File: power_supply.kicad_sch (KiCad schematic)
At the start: 24 parts, among them U3 ST1S10PHR, U4 ST1S09IPUR

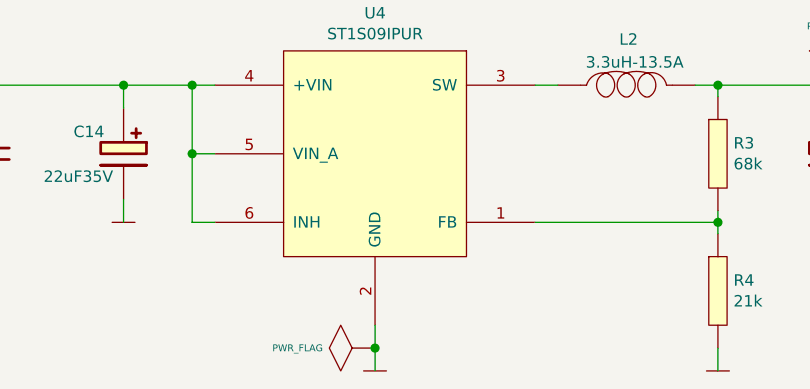
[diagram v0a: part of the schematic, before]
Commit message: Cleared all errors DRC
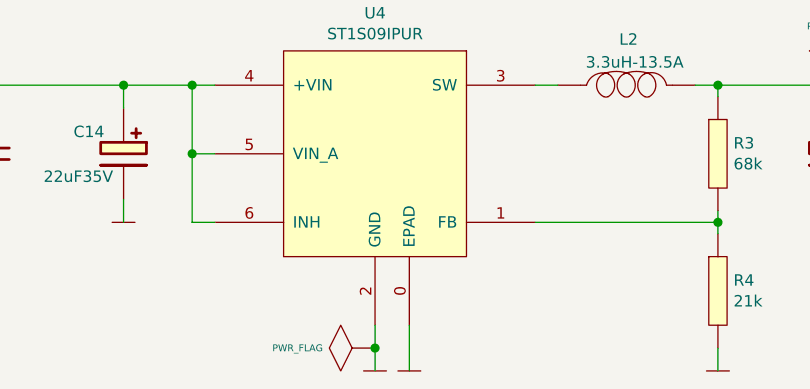
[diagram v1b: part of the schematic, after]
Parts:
- C15: symbol Capacitors_Smd0603:10nF_0603 -> Capacitors_Smd0603:10nF; Supplier TME -> Tme
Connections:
- net GND: now also U4.0 (EPAD)
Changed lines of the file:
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@@
     (stroke (width 0) (type solid) (color 0 0 0 0))
+  )
+  (wire (pts (xy 217.17 186.69) (xy 217.17 191.77))
+    (stroke (width 0) (type default) (color 0 0 0 0))
   )
   (wire (pts (xy 266.7 118.11) (xy 266.7 119.38))
@@
       (effects (font (size 1.27 1.27)) hide)
     )
+    (pin "0")
     (pin "1")
     (pin "2")
@@
     (pin "8")
   )
-  (symbol (lib_id "Capacitors_Smd0603:10nF_0603") (at 251.46 110.49 0) (unit 1)
+  (symbol (lib_id "Capacitors_Smd0603:10nF") (at 251.46 110.49 0) (unit 1)
     (in_bom yes) (on_board yes)
     (property "Reference" "C15" (id 0) (at 254.7874 109.3216 0)
@@
       (effects (font (size 1.27 1.27)) hide)
     )
-    (property "Supplier" "TME" (id 6) (at 251.46 110.49 0)
+    (property "Supplier" "Tme" (id 6) (at 251.46 110.49 0)
       (effects (font (size 1.27 1.27)) hide)
     )
@@
       (effects (font (size 1.524 1.524)))
     )
+    (pin "1")
+  )
+  (symbol (lib_id "power:GND_NO_GLOBAL") (at 217.17 191.77 0) (unit 1)
+    (in_bom yes) (on_board yes)
+    (property "Reference" "#PWR233" (id 0) (at 217.17 189.23 0)
+      (effects (font (size 0.762 0.762)) hide)
+    )
+    (property "Value" "GND_NO_GLOBAL" (id 1) (at 217.17 194.31 0)
+      (effects (font (size 0.762 0.762)) hide)
+    )
+    (property "Footprint" "" (id 2) (at 217.17 191.77 0)
+      (effects (font (size 1.524 1.524)))
+    )
+    (property "Datasheet" "" (id 3) (at 217.17 191.77 0)
+      (effects (font (size 1.524 1.524)))
+    )

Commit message: Eliminated all warnings realted with footprints
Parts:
- C10, C13, C19, C20, C7, C9: footprint Capacitors_Smd_0603:100nF_0603 -> Capacitors_Smd_0402:100nF_0402; symbol Capacitors_Smd0603:100n -> Capacitors_Smd0402:100nF; Developer (none) -> MW; LCSC Part # (optional) (none) -> C131394; Manufacturer SAMSUNG -> Murata; Manufacturer Part Number CL10B104JB8NNNC -> GRM155R71H104KE14D; Package 0603 -> 0402; Package_1 (none) -> 0402; Price@1000pcs 0,02231 -> 0,03299; Price@1pc 0,04540 -> 0,07091; Supplier TME -> Tme; Supplier Part Number CL10B104JB8NNNC -> GRM155R71H104KE14D; URL https://www.tme.eu/pl/details/cl10b104jb8nnnc/kondensatory-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 -> https://www.tme.eu/pl/details/grm155r71h104ke14d/kondensato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

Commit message: Gerbers created, BOM, CPL
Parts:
- R2, R6: Price@1pc (none) -> 0,07119
- R3: Developer (none) -> MW; Field11 MW -> (none)
- R4: Price@1pc (none) -> 0,05002
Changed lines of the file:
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@@
+      (effects (font (size 1.27 1.27)) hide)
+    )
+    (property "Price@1pc" "0,07119" (id 14) (at 266.7 125.73 0)
       (effects (font (size 1.27 1.27)) hide)
     )
@@
       (effects (font (size 1.27 1.27)) hide)
     )
-    (property "Datasheet" "Resistors/Smd_0603/Components_Documentation/Vishay_Resistors_SM0603.pdf" (id 3) (at 262.89 121.92 0)
+    (property "Datasheet" "https://www.tme.eu/Document/b315665a56acbc42df513c99b390ad98/ROYALOHM-THICKFILM.pdf" (id 3) (at 262.89 121.92 0)
       (effects (font (size 1.27 1.27)) hide)
     )
@@
     )
     (property "LCSC Part #(optional)" "C234435" (id 13) (at 186.69 114.3 0)
+      (effects (font (size 1.27 1.27)) hide)
+    )
+    (property "Price@1pc" "0,07119" (id 14) (at 186.69 114.3 0)
       (effects (font (size 1.27 1.27)) hide)
     )
@@
       (effects (font (size 1.27 1.27)) hide)
     )
+    (property "Price@1pc" "0,05002" (id 14) (at 251.46 182.88 0)
+      (effects (font (size 1.27 1.27)) hide)
+    )
     (pin "1")
     (pin "2")
@@
     )
     (property "Package" "7.2 mm x 6.65 mm x 3 mm" (id 12) (at 241.3 160.02 0)
-      (effects (font (size 1.27 1.27)) hide)
-    )
-    (pin "1")
-    (pin "2")
-  )
-  (symbol (lib_id "Resistors_Smd0603:68k") (at 251.46 167.64 0) (unit 1)
-    (in_bom yes) (on_board yes)
-    (property "Reference" "R3" (id 0) (at 253.1872 166.4716 0)
-      (effects (font (size 1.27 1.27)) (justify left))
-    )
-    (property "Value" "68k" (id 1) (at 253.1872 168.783 0)
-      (effects (font (size 1.27 1.27)) (justify left))
-    )
-    (property "Footprint" "Resistor_Smd_0603:68k_0603" (id 2) (at 251.46 179.07 0)
-      (effects (font (size 1.27 1.27)) hide)
-    )
-    (property "Datasheet" "Resistors/Smd_0603/Components_Documentation/Vishay_Resistors_SM0603.pdf" (id 3) (at 251.46 179.07 0)
-      (effects (font (size 1.27 1.27)) hide)
-    )
-    (property "Manufacturer" "ROYAL OHM" (id 4) (at 251.46 167.64 0)
-      (effects (font (size 1.27 1.27)) hide)
-    )
-    (property "Manufacturer Part Number" "0603SAF6802T5E" (id 5) (at 251.46 167.64 0)
-      (effects (font (size 1.27 1.27)) hide)
-    )
-    (property "Supplier" "TME" (id 6) (at 251.46 167.64 0)
-      (effects (font (size 1.27 1.27)) hide)
-    )
-    (property "Supplier Part Number" "SMD0603-68K-1%" (id 7) (at 251.46 167.64 0)
-      (effects (font (size 1.27 1.27)) hide)
-    )
-    (property "URL" "https://www.tme.eu/pl/details/smd0603-68k-1%2525/rezystory-smd-0603/royal-ohm/0603saf6802t5e/" (id 8) (at 251.46 167.64 0)
-      (effects (font (size 1.27 1.27)) hide)
-    )
-    (property "Price@1pc" "0,04693" (id 9) (at 251.46 167.64 0)
-      (effects (font (size 1.27 1.27)) hide)
-    )
-    (property "Price@1000pcs" "0,01269" (id 10) (at 251.46 167.64 0)
-      (effects (font (size 1.27 1.27)) hide)
-    )
-    (property "Field11" "MW" (id 11) (at 251.46 167.64 0)
-      (effects (font (size 1.27 1.27)) hide)
-    )
-    (property "Package" "0603" (id 12) (at 251.46 167.64 0)
-      (effects (font (size 1.27 1.27)) hide)
-    )
-    (property "LCSC Part #(optional)" "C160055" (id 13) (at 251.46 167.64 0)
       (effects (font (size 1.27 1.27)) hide)
     )
@@
     (pin "1")
   )
+  (symbol (lib_id "Resistors_Smd0603:68k") (at 251.46 167.64 0) (unit 1)
+    (in_bom yes) (on_board yes) (fields_autoplaced)
+    (property "Reference" "R3" (id 0) (at 253.111 166.7315 0)
+      (effects (font (size 1.27 1.27)) (justify left))
+    )
+    (property "Value" "68k" (id 1) (at 253.111 169.5066 0)
+      (effects (font (size 1.27 1.27)) (justify left))
+    )
+    (property "Footprint" "Resistor_Smd_0603:68k_0603" (id 2) (at 251.46 179.07 0)
+      (effects (font (size 1.27 1.27)) hide)
+    )
+    (property "Datasheet" "https://www.tme.eu/Document/4f50d320a6ddacb273098f84373b6259/rezystor-smd.pdf" (id 3) (at 251.46 179.07 0)
+      (effects (font (size 1.27 1.27)) hide)
+    )
+    (property "Manufacturer" "ROYAL OHM" (id 4) (at 251.46 167.64 0)
+      (effects (font (size 1.27 1.27)) hide)
+    )
+    (property "Manufacturer Part Number" "0603SAF6802T5E" (id 5) (at 251.46 167.64 0)
+      (effects (font (size 1.27 1.27)) hide)
+    )
+    (property "Supplier" "TME" (id 6) (at 251.46 167.64 0)
+      (effects (font (size 1.27 1.27)) hide)
+    )
+    (property "Supplier Part Number" "SMD0603-68K-1%" (id 7) (at 251.46 167.64 0)
+      (effects (font (size 1.27 1.27)) hide)
+    )
+    (property "URL" "https://www.tme.eu/pl/details/smd0603-68k-1%2525/rezystory-smd-0603/royal-ohm/0603saf6802t5e/" (id 8) (at 251.46 167.64 0)
+      (effects (font (size 1.27 1.27)) hide)
+    )
+    (property "Price@1pc" "0,04693" (id 9) (at 251.46 167.64 0)
+      (effects (font (size 1.27 1.27)) hide)
+    )
+    (property "Price@1000pcs" "0,01269" (id 10) (at 251.46 167.64 0)
+      (effects (font (size 1.27 1.27)) hide)
+    )
+    (property "Developer" "MW" (id 11) (at 251.46 167.64 0)
+      (effects (font (size 1.27 1.27)) hide)
+    )
+    (property "Package" "0603" (id 12) (at 251.46 167.64 0)
+      (effects (font (size 1.27 1.27)) hide)
+    )
+    (property "LCSC Part #(optional)" "C160055" (id 13) (at 251.46 167.64 0)
+      (effects (font (size 1.27 1.27)) hide)
+    )
+    (pin "1")
+    (pin "2")
+  )
   (symbol (lib_id "power:GND_NO_GLOBAL") (at 217.17 191.77 0) (unit 1)
